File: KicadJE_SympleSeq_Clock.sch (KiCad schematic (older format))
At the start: 31 parts, among them J201 clk_in, J202 clk_out, J203 Hold, J204 Reset, P201 HEADER_2x5_Doepfer, U201 LM555, U202 4017

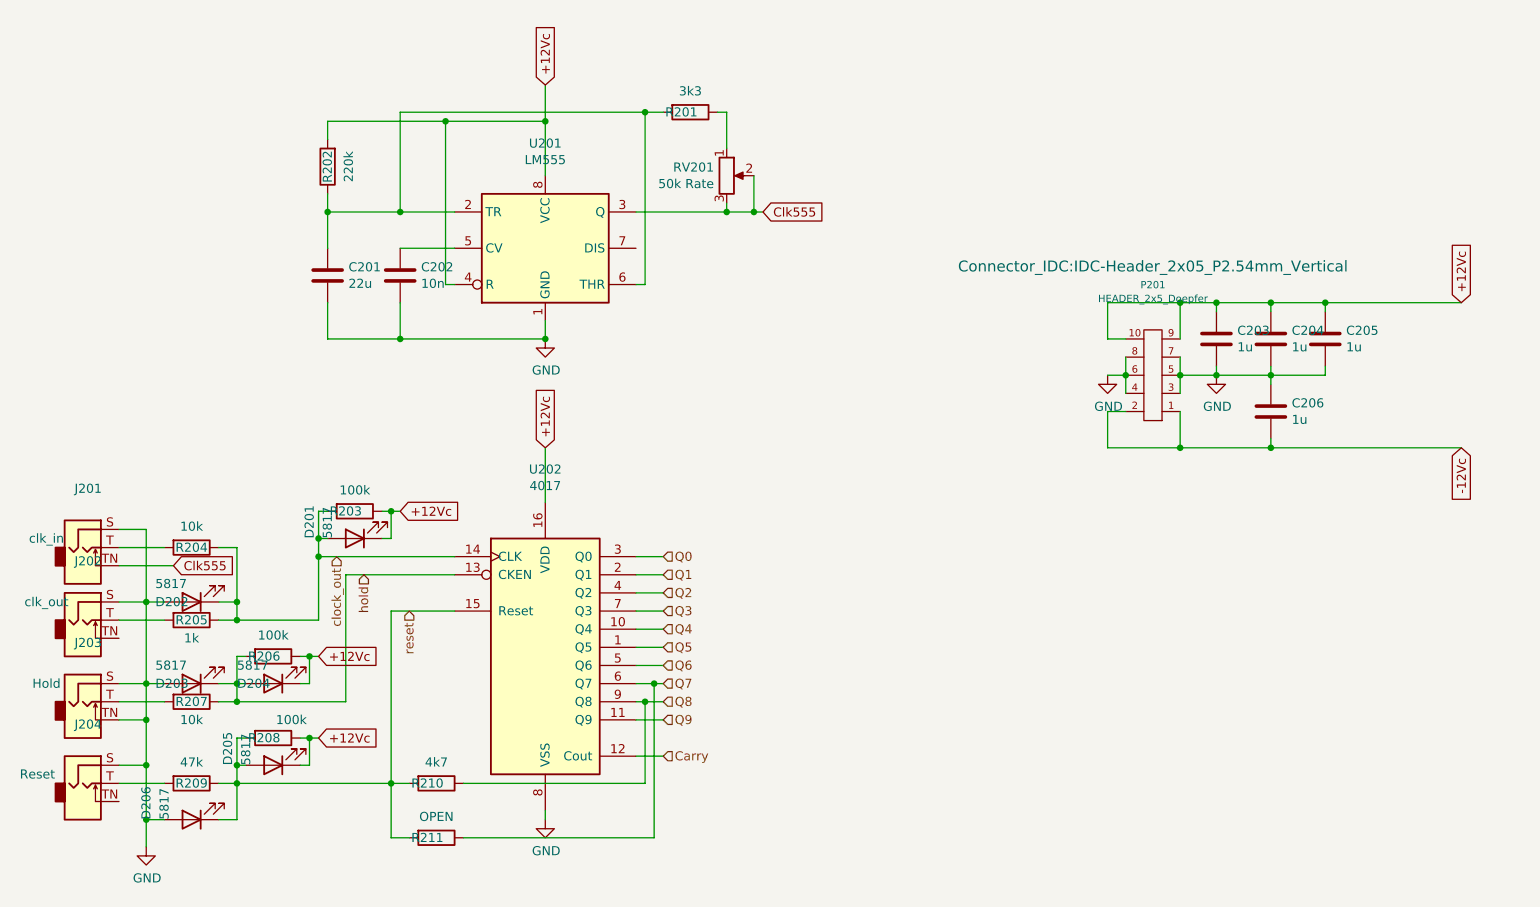
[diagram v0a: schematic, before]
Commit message: slave clk - debounce hold etc
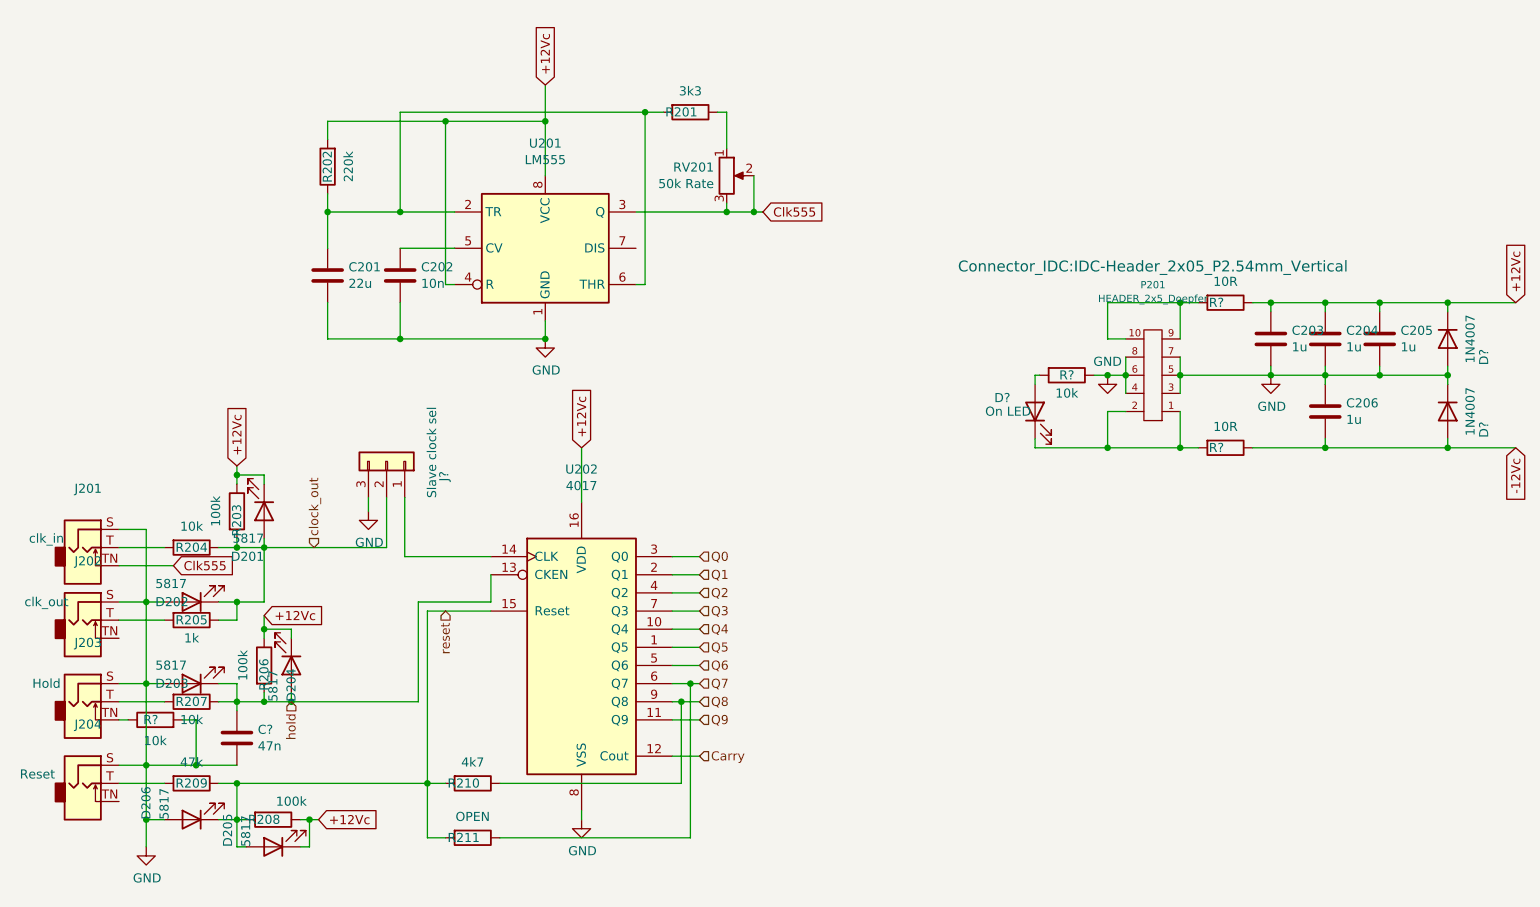
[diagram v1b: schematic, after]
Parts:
- added C?: 47n, Capacitor_SMD:C_0805_2012Metric_Pad1.15x1.40mm_HandSolder, symbol Device:C
- added D? (x2): 1N4007, Diode_SMD:D_MiniMELF, symbol Diode:LL4148
- added D?: On LED, LED_SMD:LED_0805_2012Metric, symbol Device:LED
- added J?: Slave clock sel, Connector_PinHeader_2.54mm:PinHeader_1x03_P2.54mm_Vertical, symbol Connector_Generic:Conn_01x03
- added R? (x2): 10R, Resistor_SMD:R_0805_2012Metric_Pad1.15x1.40mm_HandSolder, symbol Device:R
- added R? (x2): 10k, Resistor_SMD:R_0805_2012Metric_Pad1.15x1.40mm_HandSolder, symbol Device:R
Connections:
- net +12Vc: now also D?.1 (K), R?.1; no longer P201.10 (+12), P201.9 (+12)
- net -12Vc: now also D?.2 (A), R?.1; no longer P201.1 (-12), P201.2 (-12)
- net GND: now also C?.2, D?.1 (K), D?.2 (A), J?.3 (Pin_3), R?.1, R?.2; no longer J203.TN
- net clock_out: now also J?.2 (Pin_2); no longer U202.14 (CLK)
- net hold: now also C?.1
- new net: J?.1 (Pin_1), U202.14 (CLK)
- new net: D?.1 (K), P201.1 (-12), P201.2 (-12), R?.2
- new net: P201.10 (+12), P201.9 (+12), R?.2
- new net: J203.TN, R?.1
- new net: D?.2 (A), R?.2
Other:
- moved on the sheet: C203, C204, C205, C206, D201, D204, D205, R203, R206, R208, R210, R211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

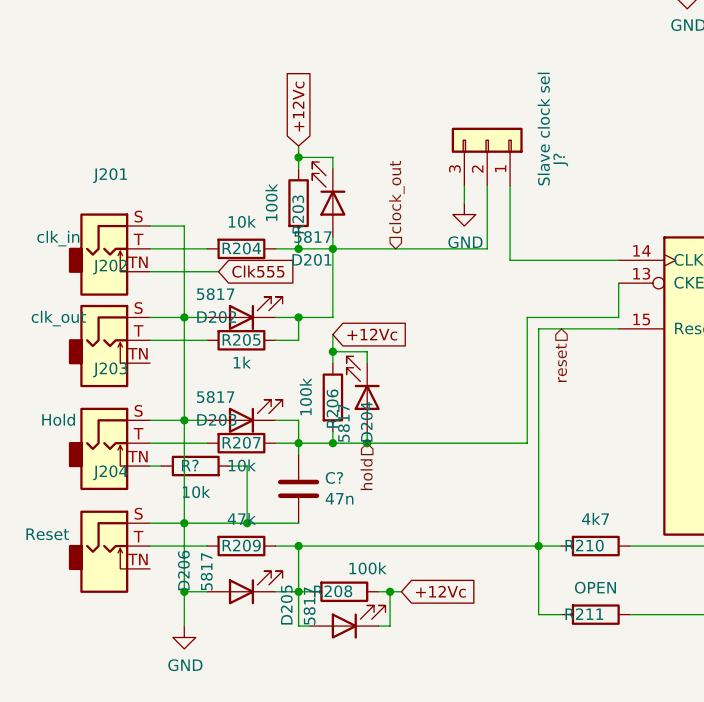
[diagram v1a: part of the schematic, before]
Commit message: Diode prot from LED->1N4007
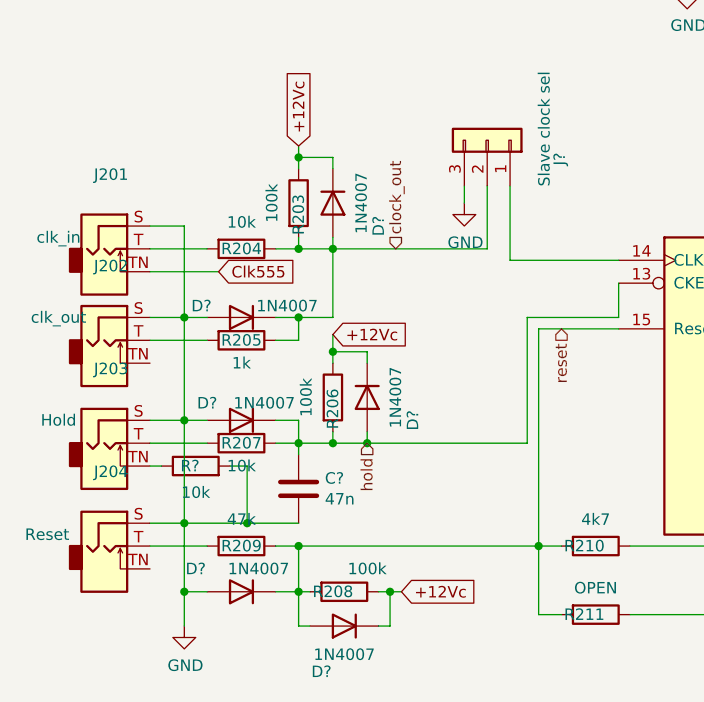
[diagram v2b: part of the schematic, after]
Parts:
- removed D201, D202, D203, D204, D205, D206: 5817, LED_SMD:LED_0805_2012Metric, symbol Device:LED
- added D? (x6): 1N4007, Diode_SMD:D_MiniMELF, symbol Diode:LL4148
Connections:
- net +12Vc: now also D?.1 (K), D?.1 (K), D?.1 (K)
- net GND: now also D?.2 (A), D?.2 (A), D?.2 (A)
- net clock_out: now also D?.1 (K), D?.2 (A)
- net hold: now also D?.1 (K), D?.2 (A)
- net reset: now also D?.1 (K), D?.2 (A)
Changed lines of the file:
@@
 	1650 5050 1650 5200
 Connection ~ 1650 4850
-$Comp
-L Device:LED D?
-U 1 1 5D9DC97C
-P 1850 5200
-AR Path="/5C8BFBBC/5D9DC97C" Ref="D?"  Part="1"
-AR Path="/5C8C5FC0/5D9DC97C" Ref="D205"  Part="1"
-F 0 "D205" V 2100 5200 50  0000 R CNN
-F 1 "5817" V 2000 5200 50  0000 R CNN
-F 2 "LED_SMD:LED_0805_2012Metric" H 1850 5200 50  0001 C CNN
-F 3 "~" H 1850 5200 50  0001 C CNN
-	1    1850 5200
-	-1   0    0    1
-$EndComp
 Wire Wire Line
 	2000 5200 2050 5200
@@
 Wire Wire Line
 	1700 5200 1650 5200
-$Comp
-L Device:LED D?
-U 1 1 5D9E8314
-P 1800 3350
-AR Path="/5C8BFBBC/5D9E8314" Ref="D?"  Part="1"
-AR Path="/5C8C5FC0/5D9E8314" Ref="D201"  Part="1"
-F 0 "D201" V 2050 3350 50  0000 R CNN
-F 1 "5817" V 1950 3350 50  0000 R CNN
-F 2 "LED_SMD:LED_0805_2012Metric" H 1800 3350 50  0001 C CNN
-F 3 "~" H 1800 3350 50  0001 C CNN
-	1    1800 3350
-	0    1    1    0
-$EndComp
 Wire Wire Line
 	1800 3200 1800 3150
 Wire Wire Line
 	1800 3150 1650 3150
-$Comp
-L Device:LED D?
-U 1 1 5D9EB48D
-P 1400 5050
-AR Path="/5C8BFBBC/5D9EB48D" Ref="D?"  Part="1"
-AR Path="/5C8C5FC0/5D9EB48D" Ref="D206"  Part="1"
-F 0 "D206" V 1650 5050 50  0000 R CNN
-F 1 "5817" V 1550 5050 50  0000 R CNN
-F 2 "LED_SMD:LED_0805_2012Metric" H 1400 5050 50  0001 C CNN
-F 3 "~" H 1400 5050 50  0001 C CNN
-	1    1400 5050
-	-1   0    0    1
-$EndComp
 Wire Wire Line
 	1550 5050 1650 5050
@@
 Wire Wire Line
 	1150 5050 1150 5200
-$Comp
-L Device:LED D?
-U 1 1 5D9F8118
-P 1400 3850
-AR Path="/5C8BFBBC/5D9F8118" Ref="D?"  Part="1"
-AR Path="/5C8C5FC0/5D9F8118" Ref="D202"  Part="1"
-F 0 "D202" H 1600 3850 50  0000 R CNN
-F 1 "5817" H 1600 3750 50  0000 R CNN
-F 2 "LED_SMD:LED_0805_2012Metric" H 1400 3850 50  0001 C CNN
-F 3 "~" H 1400 3850 50  0001 C CNN
-	1    1400 3850
-	-1   0    0    1
-$EndComp
 Wire Wire Line
 	1550 3850 1650 3850
 Wire Wire Line
 	1250 3850 1150 3850
-$Comp
-L Device:LED D?
-U 1 1 5D9FFDB2
-P 1950 4200
-AR Path="/5C8BFBBC/5D9FFDB2" Ref="D?"  Part="1"
-AR Path="/5C8C5FC0/5D9FFDB2" Ref="D204"  Part="1"
-F 0 "D204" H 2150 4200 50  0000 R CNN
-F 1 "5817" H 2150 4100 50  0000 R CNN
-F 2 "LED_SMD:LED_0805_2012Metric" H 1950 4200 50  0001 C CNN
-F 3 "~" H 1950 4200 50  0001 C CNN
-	1    1950 4200
-	0    1    1    0
-$EndComp
 Wire Wire Line
 	1950 4350 1950 4400
@@
 	1650 3150 1650 3100
 Connection ~ 1650 3150
-$Comp
-L Device:LED D?
-U 1 1 5DA158FD
-P 1400 4300
-AR Path="/5C8BFBBC/5DA158FD" Ref="D?"  Part="1"
-AR Path="/5C8C5FC0/5DA158FD" Ref="D203"  Part="1"
-F 0 "D203" H 1600 4300 50  0000 R CNN
-F 1 "5817" H 1600 4200 50  0000 R CNN
-F 2 "LED_SMD:LED_0805_2012Metric" H 1400 4300 50  0001 C CNN
-F 3 "~" H 1400 4300 50  0001 C CNN
-	1    1400 4300
-	-1   0    0    1
-$EndComp
 Wire Wire Line
 	1250 4300 1150 4300
@@
 Wire Wire Line
 	1425 4750 1150 4750
+$Comp
+L Diode:LL4148 D?
+U 1 1 5EBEA1D6
+P 1800 3350
+AR Path="/5C8BFBBC/5EBEA1D6" Ref="D?"  Part="1"
+AR Path="/5C8C5FC0/5EBEA1D6" Ref="D?"  Part="1"
+F 0 "D?" H 1900 3550 50  0000 C CNN
+F 1 "1N4007" H 1800 3475 50  0000 C CNN
+F 2 "Diode_SMD:D_MiniMELF" H 1800 3175 50  0001 C CNN
+F 3 "http://www.vishay.com/docs/85557/ll4148.pdf" H 1800 3350 50  0001 C CNN
+	1    1800 3350
+	0    1    1    0
+$EndComp
+$Comp
+L Diode:LL4148 D?
+U 1 1 5EBEB078
+P 1950 4200
+AR Path="/5C8BFBBC/5EBEB078" Ref="D?"  Part="1"
+AR Path="/5C8C5FC0/5EBEB078" Ref="D?"  Part="1"
+F 0 "D?" H 2050 4400 50  0000 C CNN
+F 1 "1N4007" H 1950 4325 50  0000 C CNN
+F 2 "Diode_SMD:D_MiniMELF" H 1950 4025 50  0001 C CNN
+F 3 "http://www.vishay.com/docs/85557/ll4148.pdf" H 1950 4200 50  0001 C CNN
+	1    1950 4200
+	0    1    1    0
+$EndComp
+$Comp
+L Diode:LL4148 D?
+U 1 1 5EBEBAE3
+P 1400 3850
+AR Path="/5C8BFBBC/5EBEBAE3" Ref="D?"  Part="1"
+AR Path="/5C8C5FC0/5EBEBAE3" Ref="D?"  Part="1"
+F 0 "D?" H 1575 3800 50  0000 C CNN
+F 1 "1N4007" H 1200 3800 50  0000 C CNN
+F 2 "Diode_SMD:D_MiniMELF" H 1400 3675 50  0001 C CNN
+F 3 "http://www.vishay.com/docs/85557/ll4148.pdf" H 1400 3850 50  0001 C CNN
+	1    1400 3850
+	-1   0    0    1
+$EndComp
+$Comp
+L Diode:LL4148 D?
+U 1 1 5EBECD23
+P 1400 4300
+AR Path="/5C8BFBBC/5EBECD23" Ref="D?"  Part="1"
+AR Path="/5C8C5FC0/5EBECD23" Ref="D?"  Part="1"
+F 0 "D?" H 1550 4225 50  0000 C CNN
+F 1 "1N4007" H 1300 4225 50  0000 C CNN
+F 2 "Diode_SMD:D_MiniMELF" H 1400 4125 50  0001 C CNN
+F 3 "http://www.vishay.com/docs/85557/ll4148.pdf" H 1400 4300 50  0001 C CNN
+	1    1400 4300
+	-1   0    0    1
+$EndComp
+$Comp
+L Diode:LL4148 D?
+U 1 1 5EBED263
+P 1400 5050
+AR Path="/5C8BFBBC/5EBED263" Ref="D?"  Part="1"
+AR Path="/5C8C5FC0/5EBED263" Ref="D?"  Part="1"
+F 0 "D?" H 1600 4950 50  0000 C CNN
+F 1 "1N4007" H 1325 4950 50  0000 C CNN
+F 2 "Diode_SMD:D_MiniMELF" H 1400 4875 50  0001 C CNN
+F 3 "http://www.vishay.com/docs/85557/ll4148.pdf" H 1400 5050 50  0001 C CNN
+	1    1400 5050
+	-1   0    0    1
+$EndComp
+$Comp
+L Diode:LL4148 D?
+U 1 1 5EBED6F5
+P 1850 5200
+AR Path="/5C8BFBBC/5EBED6F5" Ref="D?"  Part="1"
+AR Path="/5C8C5FC0/5EBED6F5" Ref="D?"  Part="1"
+F 0 "D?" H 1950 5400 50  0000 C CNN
+F 1 "1N4007" H 1850 5325 50  0000 C CNN
+F 2 "Diode_SMD:D_MiniMELF" H 1850 5025 50  0001 C CNN
+F 3 "http://www.vishay.com/docs/85557/ll4148.pdf" H 1850 5200 50  0001 C CNN
+	1    1850 5200
+	-1   0    0    1
+$EndComp
 $EndSCHEMATC

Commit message: ERC Rev B
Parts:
- gave numbers to parts that had none: 15
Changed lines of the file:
@@
 Connection ~ 7650 2200
 Wire Wire Line
-	7650 3000 8325 3000
+	7650 3000 8150 3000
 Connection ~ 7650 3000
 $Comp
@@
 Connection ~ 7950 2200
 Wire Wire Line
-	7950 2200 8325 2200
+	7950 2200 8150 2200
 Wire Wire Line
 	7950 2550 7950 2600
@@
 P 8325 2400
 AR Path="/5C8BFBBC/5EAA4FDE" Ref="D?"  Part="1"
-AR Path="/5C8C5FC0/5EAA4FDE" Ref="D?"  Part="1"
-F 0 "D?" H 8425 2600 50  0000 C CNN
+AR Path="/5C8C5FC0/5EAA4FDE" Ref="D208"  Part="1"
+F 0 "D208" H 8425 2600 50  0000 C CNN
 F 1 "1N4007" H 8325 2525 50  0000 C CNN
 F 2 "Diode_SMD:D_MiniMELF" H 8325 2225 50  0001 C CNN
@@
 P 8325 2800
 AR Path="/5C8BFBBC/5EAAADA1" Ref="D?"  Part="1"
-AR Path="/5C8C5FC0/5EAAADA1" Ref="D?"  Part="1"
-F 0 "D?" H 8425 3000 50  0000 C CNN
+AR Path="/5C8C5FC0/5EAAADA1" Ref="D209"  Part="1"
+F 0 "D209" H 8425 3000 50  0000 C CNN
 F 1 "1N4007" H 8325 2925 50  0000 C CNN
 F 2 "Diode_SMD:D_MiniMELF" H 8325 2625 50  0001 C CNN
@@
 P 7100 2200
 AR Path="/5EAD1F8B" Ref="R?"  Part="1"
-AR Path="/5C8C5FC0/5EAD1F8B" Ref="R?"  Part="1"
-F 0 "R?" V 7100 2150 50  0000 C CNN
+AR Path="/5C8C5FC0/5EAD1F8B" Ref="R214"  Part="1"
+F 0 "R214" V 7100 2150 50  0000 C CNN
 F 1 "10R" V 6984 2200 50  0000 C CNN
 F 2 "Resistor_SMD:R_0805_2012Metric_Pad1.15x1.40mm_HandSolder" V 7030 2200 50  0001 C CNN
@@
 P 7100 3000
 AR Path="/5EAD2AD8" Ref="R?"  Part="1"
-AR Path="/5C8C5FC0/5EAD2AD8" Ref="R?"  Part="1"
-F 0 "R?" V 7100 2950 50  0000 C CNN
+AR Path="/5C8C5FC0/5EAD2AD8" Ref="R215"  Part="1"
+F 0 "R215" V 7100 2950 50  0000 C CNN
 F 1 "10R" V 6984 3000 50  0000 C CNN
 F 2 "Resistor_SMD:R_0805_2012Metric_Pad1.15x1.40mm_HandSolder" V 7030 3000 50  0001 C CNN
@@
 P 6050 2800
 AR Path="/5C8BFBBC/5EAD369C" Ref="D?"  Part="1"
-AR Path="/5C8C5FC0/5EAD369C" Ref="D?"  Part="1"
-F 0 "D?" V 6125 3025 50  0000 R CNN
+AR Path="/5C8C5FC0/5EAD369C" Ref="D207"  Part="1"
+F 0 "D207" V 6125 3025 50  0000 R CNN
 F 1 "On LED" V 6050 3075 50  0000 R CNN
 F 2 "LED_SMD:LED_0805_2012Metric" H 6050 2800 50  0001 C CNN
@@
 P 6225 2600
 AR Path="/5EAD4374" Ref="R?"  Part="1"
-AR Path="/5C8C5FC0/5EAD4374" Ref="R?"  Part="1"
-F 0 "R?" V 6225 2600 50  0000 C CNN
+AR Path="/5C8C5FC0/5EAD4374" Ref="R213"  Part="1"
+F 0 "R213" V 6225 2600 50  0000 C CNN
 F 1 "10k" V 6325 2600 50  0000 C CNN
 F 2 "Resistor_SMD:R_0805_2012Metric_Pad1.15x1.40mm_HandSolder" V 6155 2600 50  0001 C CNN
@@
 	1800 3550 2475 3550
 $Comp
-L Device:C C?
+L Device:C C207
 U 1 1 5EB2E111
 P 1650 4600
-F 0 "C?" H 1765 4646 50  0000 L CNN
+F 0 "C207" H 1765 4646 50  0000 L CNN
 F 1 "47n" H 1765 4555 50  0000 L CNN
 F 2 "Capacitor_SMD:C_0805_2012Metric_Pad1.15x1.40mm_HandSolder" H 1688 4450 50  0001 C CNN
@@
 P 2475 3075
 AR Path="/5EB64ADC" Ref="J?"  Part="1"
-AR Path="/5C8C5FC0/5EB64ADC" Ref="J?"  Part="1"
-F 0 "J?" H 2393 3392 50  0000 C CNN
+AR Path="/5C8C5FC0/5EB64ADC" Ref="J205"  Part="1"
+F 0 "J205" H 2393 3392 50  0000 C CNN
 F 1 "Slave clock sel" H 2525 3325 50  0000 C CNN
 F 2 "Connector_PinHeader_2.54mm:PinHeader_1x03_P2.54mm_Vertical" H 2475 3075 50  0001 C CNN
@@
 P 2375 3350
 AR Path="/5EB8117E" Ref="#PWR?"  Part="1"
-AR Path="/5C8C5FC0/5EB8117E" Ref="#PWR?"  Part="1"
-F 0 "#PWR?" H 2375 3100 50  0001 C CNN
+AR Path="/5C8C5FC0/5EB8117E" Ref="#PWR0204"  Part="1"
+F 0 "#PWR0204" H 2375 3100 50  0001 C CNN
 F 1 "GND" H 2380 3177 50  0000 C CNN
 F 2 "" H 2375 3350 50  0001 C CNN
@@
 P 1200 4500
 AR Path="/5EBB45A6" Ref="R?"  Part="1"
-AR Path="/5C8C5FC0/5EBB45A6" Ref="R?"  Part="1"
-F 0 "R?" V 1200 4525 50  0000 C CNN
+AR Path="/5C8C5FC0/5EBB45A6" Ref="R212"  Part="1"
+F 0 "R212" V 1200 4525 50  0000 C CNN
 F 1 "10k" V 1084 4500 50  0000 C CNN
 F 2 "Resistor_SMD:R_0805_2012Metric_Pad1.15x1.40mm_HandSolder" V 1130 4500 50  0001 C CNN
@@
 P 1800 3350
 AR Path="/5C8BFBBC/5EBEA1D6" Ref="D?"  Part="1"
-AR Path="/5C8C5FC0/5EBEA1D6" Ref="D?"  Part="1"
-F 0 "D?" H 1900 3550 50  0000 C CNN
+AR Path="/5C8C5FC0/5EBEA1D6" Ref="D204"  Part="1"
+F 0 "D204" H 1900 3550 50  0000 C CNN
 F 1 "1N4007" H 1800 3475 50  0000 C CNN
 F 2 "Diode_SMD:D_MiniMELF" H 1800 3175 50  0001 C CNN
@@
 P 1950 4200
 AR Path="/5C8BFBBC/5EBEB078" Ref="D?"  Part="1"
-AR Path="/5C8C5FC0/5EBEB078" Ref="D?"  Part="1"
-F 0 "D?" H 2050 4400 50  0000 C CNN
+AR Path="/5C8C5FC0/5EBEB078" Ref="D206"  Part="1"
+F 0 "D206" H 2050 4400 50  0000 C CNN
 F 1 "1N4007" H 1950 4325 50  0000 C CNN
 F 2 "Diode_SMD:D_MiniMELF" H 1950 4025 50  0001 C CNN
@@
 P 1400 3850
 AR Path="/5C8BFBBC/5EBEBAE3" Ref="D?"  Part="1"
-AR Path="/5C8C5FC0/5EBEBAE3" Ref="D?"  Part="1"
-F 0 "D?" H 1575 3800 50  0000 C CNN
+AR Path="/5C8C5FC0/5EBEBAE3" Ref="D201"  Part="1"
+F 0 "D201" H 1575 3800 50  0000 C CNN
 F 1 "1N4007" H 1200 3800 50  0000 C CNN
 F 2 "Diode_SMD:D_MiniMELF" H 1400 3675 50  0001 C CNN
@@
 P 1400 4300
 AR Path="/5C8BFBBC/5EBECD23" Ref="D?"  Part="1"
-AR Path="/5C8C5FC0/5EBECD23" Ref="D?"  Part="1"
-F 0 "D?" H 1550 4225 50  0000 C CNN
+AR Path="/5C8C5FC0/5EBECD23" Ref="D202"  Part="1"
+F 0 "D202" H 1550 4225 50  0000 C CNN
 F 1 "1N4007" H 1300 4225 50  0000 C CNN
 F 2 "Diode_SMD:D_MiniMELF" H 1400 4125 50  0001 C CNN
@@
 P 1400 5050
 AR Path="/5C8BFBBC/5EBED263" Ref="D?"  Part="1"
-AR Path="/5C8C5FC0/5EBED263" Ref="D?"  Part="1"
-F 0 "D?" H 1600 4950 50  0000 C CNN
+AR Path="/5C8C5FC0/5EBED263" Ref="D203"  Part="1"
+F 0 "D203" H 1600 4950 50  0000 C CNN
 F 1 "1N4007" H 1325 4950 50  0000 C CNN
 F 2 "Diode_SMD:D_MiniMELF" H 1400 4875 50  0001 C CNN
@@
 P 1850 5200
 AR Path="/5C8BFBBC/5EBED6F5" Ref="D?"  Part="1"
-AR Path="/5C8C5FC0/5EBED6F5" Ref="D?"  Part="1"
-F 0 "D?" H 1950 5400 50  0000 C CNN
+AR Path="/5C8C5FC0/5EBED6F5" Ref="D205"  Part="1"
+F 0 "D205" H 1950 5400 50  0000 C CNN
 F 1 "1N4007" H 1850 5325 50  0000 C CNN
 F 2 "Diode_SMD:D_MiniMELF" H 1850 5025 50  0001 C CNN
@@
 	-1   0    0    1
 $EndComp
+$Comp
+L power:PWR_FLAG #FLG0101
+U 1 1 5EBEF9D0
+P 6450 2600
+F 0 "#FLG0101" H 6450 2675 50  0001 C CNN
+F 1 "PWR_FLAG" H 6450 2773 50  0000 C CNN
+F 2 "" H 6450 2600 50  0001 C CNN
+F 3 "~" H 6450 2600 50  0001 C CNN
+	1    6450 2600
+	1    0    0    -1
+$EndComp
+$Comp
+L power:PWR_FLAG #FLG0102
+U 1 1 5EBF05AF
+P 8150 2200
+F 0 "#FLG0102" H 8150 2275 50  0001 C CNN
+F 1 "PWR_FLAG" H 8150 2373 50  0000 C CNN
+F 2 "" H 8150 2200 50  0001 C CNN
+F 3 "~" H 8150 2200 50  0001 C CNN
+	1    8150 2200
+	1    0    0    -1
+$EndComp
+Connection ~ 8150 2200
+Wire Wire Line
+	8150 2200 8325 2200
+$Comp
+L power:PWR_FLAG #FLG0103
+U 1 1 5EBF12D2
+P 8150 3000
+F 0 "#FLG0103" H 8150 3075 50  0001 C CNN
+F 1 "PWR_FLAG" H 8150 3173 50  0000 C CNN
+F 2 "" H 8150 3000 50  0001 C CNN
+F 3 "~" H 8150 3000 50  0001 C CNN
+	1    8150 3000
+	1    0    0    -1
+$EndComp
+Connection ~ 8150 3000
+Wire Wire Line
+	8150 3000 8325 3000
 $EndSCHEMATC
